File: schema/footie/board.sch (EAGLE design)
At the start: 35 parts, among them T1 2N3565, U1 ATMEGA328P-MU, U2 USD-SOCKETNEW, U3 HC_05, U4 MCP73831, U5 3.3 regulator, Y1 8MHZ

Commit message: complete the first pcb version
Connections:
- net GND renamed N$22
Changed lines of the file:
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@@
 </busses>
 <nets>
-<net name="GND" class="0">
+<net name="N$22" class="0">
 <segment>
 <pinref part="U$1" gate="G$1" pin="24_GND"/>

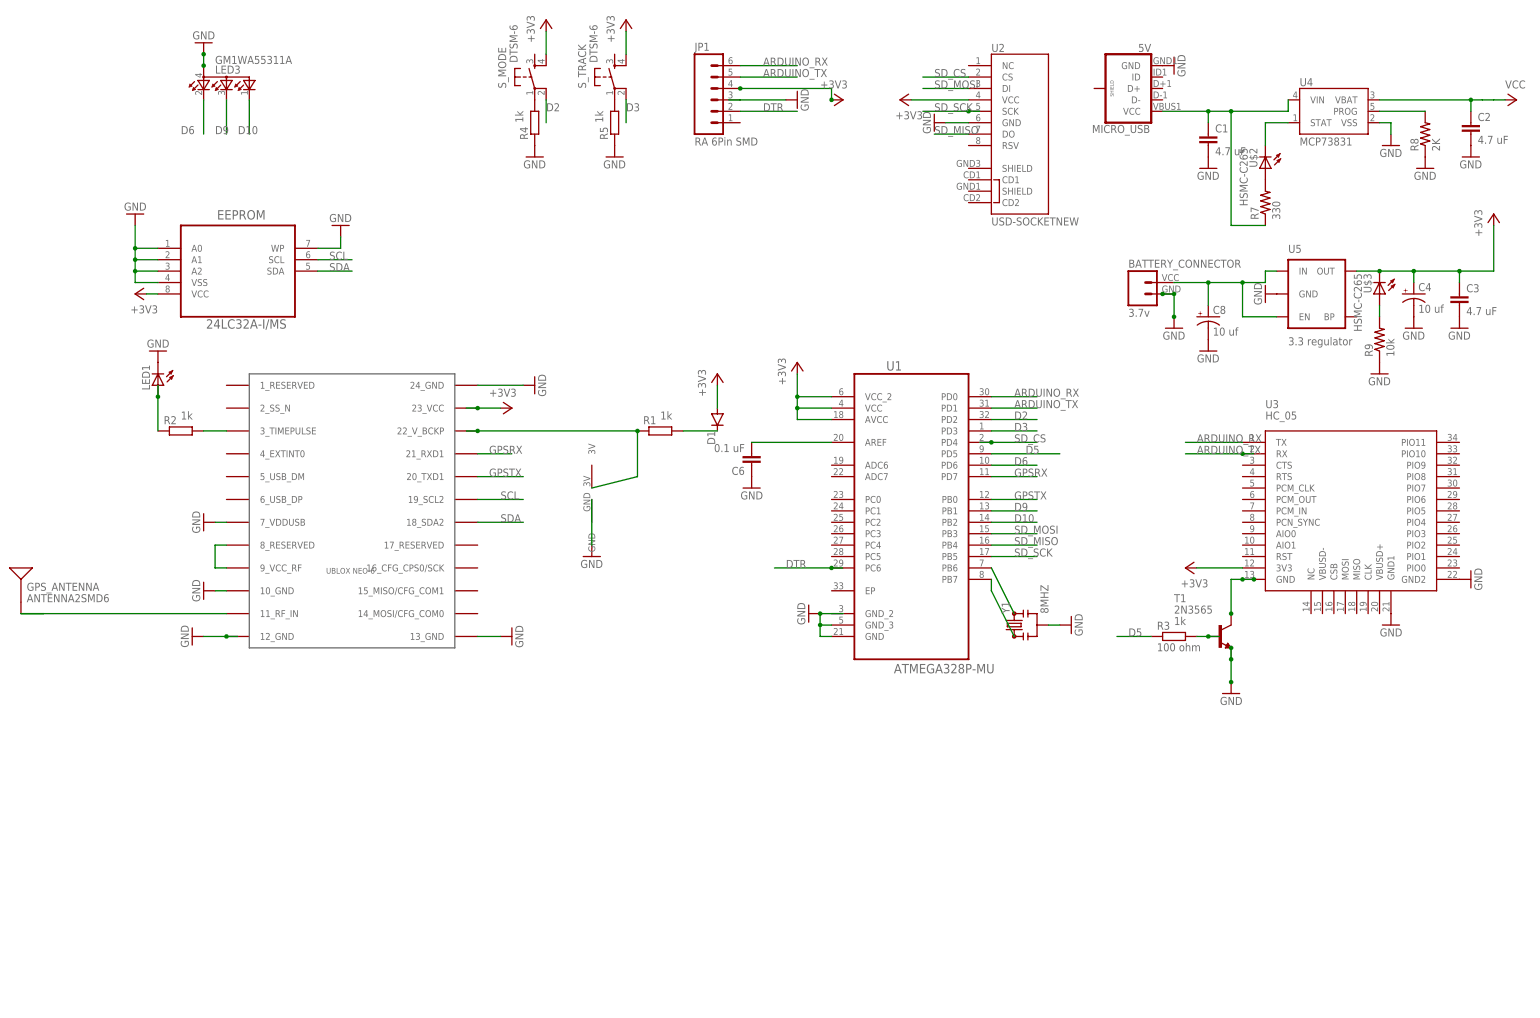
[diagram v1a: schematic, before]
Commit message: update items to 1206 package update cpu update library
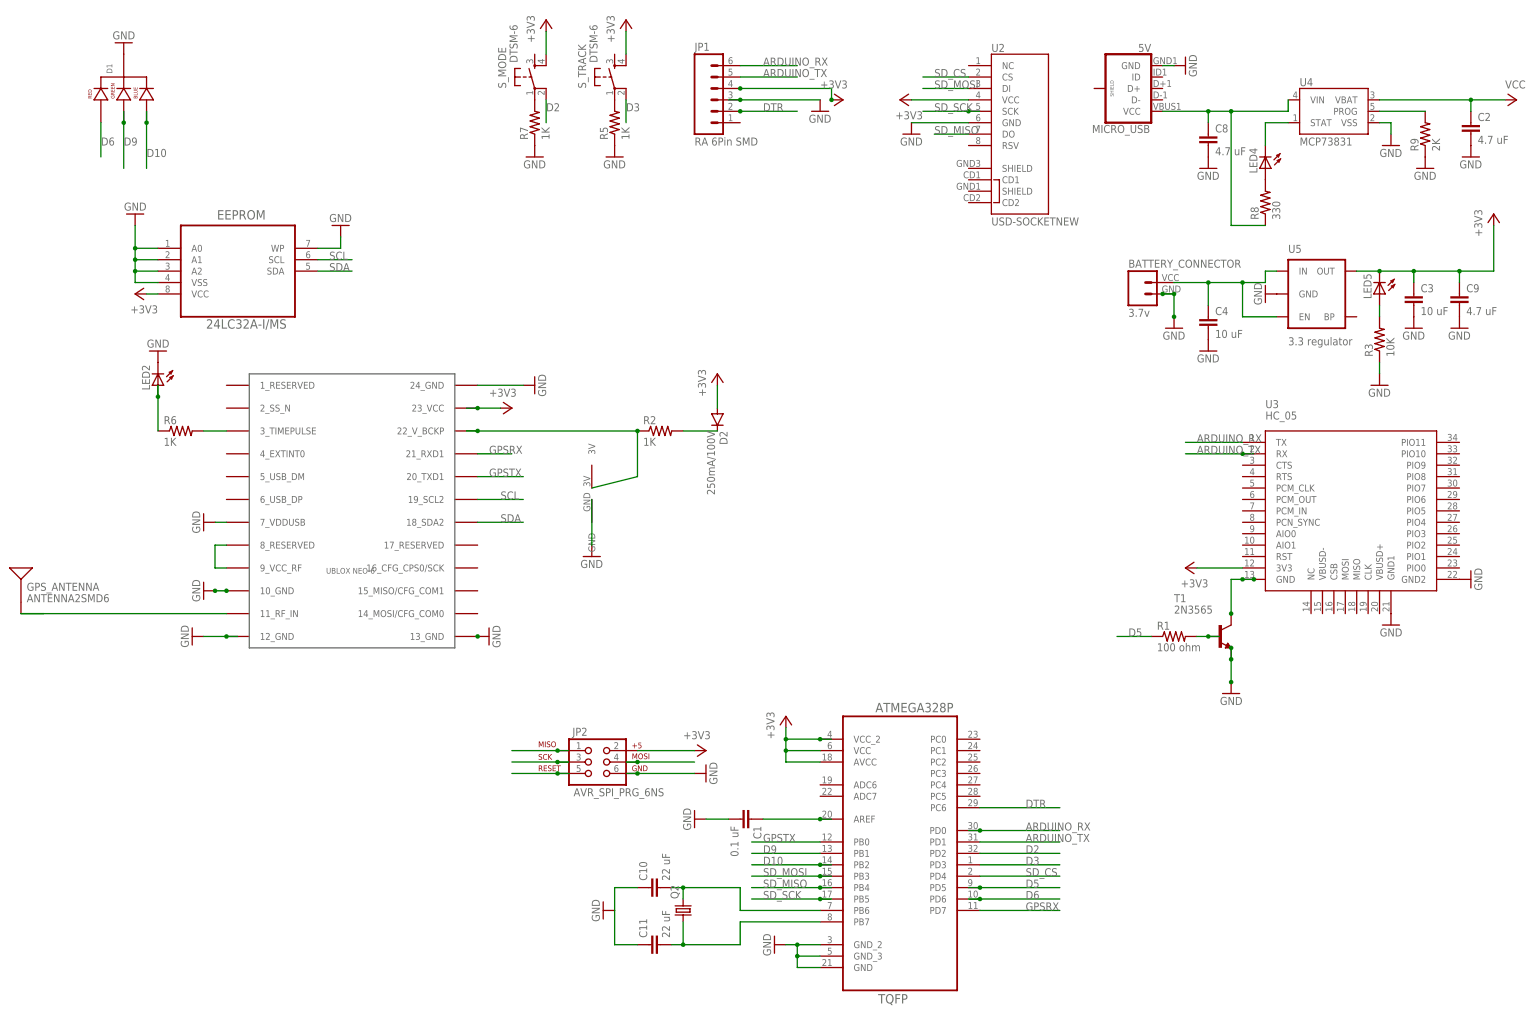
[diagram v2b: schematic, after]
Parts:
- removed C6: 0.1 uF, resistor:C-EUC0402K
- removed LED1: (no value), led:LEDCHIP-LED0805
- removed LED3: GM1WA55311A, led:GM1WA55311A
- removed R4: (no value), resistor:R-EU_M1406
- removed U$2, U$3: HSMC-C265, SparkFun-Retired:HSMC-C265
- removed U1: ATMEGA328P-MU, Atmel_By_element14_Batch_1-00:ATMEGA328P-MU
- removed Y1: 8MHZ, SparkFun-FreqCtrl:RESONATOR16MHZ
- added C10, C11: 22 uF, SparkFun-Capacitors:CAP1206
- added C9: 4.7 uF, SparkFun-Capacitors:CAP1206
- added D2: 250mA/100V, SparkFun-DiscreteSemi:DIODEBAS16
- added JP2: AVR_SPI_PRG_6NS, SparkFun-Connectors:AVR_SPI_PRG_6NS
- added LED2, LED4, LED5: (no value), eagle-ltspice:LED_E
- added Q2: (no value), crystal:CRYSTALCTS406
- added R6: 1K, SparkFun-Passives:RESISTOR1206
- added U6: ATMEGA328P-AU, Ava:ATMEGA328P-AU
- C1: value 4.7 uF -> 0.1 uF; device resistor:C-EUC0402K -> SparkFun-Capacitors:CAP1206
- C2: device resistor:C-EUC0402K -> SparkFun-Capacitors:CAP1206
- C3: value 4.7 uF -> 10 uF; device resistor:C-EUC0402K -> SparkFun-Capacitors:CAP1206
- C4: value 10 uf -> 10 uF; device resistor:CPOL-USA -> SparkFun-Capacitors:CAP1206
- C8: value 10 uf -> 4.7 uF; device resistor:CPOL-USA -> SparkFun-Capacitors:CAP1206
- D1: value (none) -> LED-RGB-CC-THRUCLEAR; device SparkFun-DiscreteSemi:DIODESMA -> SparkFun-LED:LED-RGB-CC-THRUCLEAR
- R1: value (none) -> 100 ohm; device resistor:R-EU_M1406 -> SparkFun-Passives:RESISTOR1206; OHM 1k -> (none)
- R2, R5: value (none) -> 1K; device resistor:R-EU_M1406 -> SparkFun-Passives:RESISTOR1206; OHM 1k -> (none)
- R3: value 100 ohm -> 10K; device resistor:R-EU_M1406 -> SparkFun-Passives:RESISTOR1206; OHM 1k -> (none)
- R7: value 330 -> 1K; device SparkFun-Passives:RESISTOR0402-RES -> SparkFun-Passives:RESISTOR1206
- R8: value 2K -> 330; device SparkFun-Passives:RESISTOR0402-RES -> SparkFun-Passives:RESISTOR1206
- R9: value 10k -> 2K; device SparkFun-Passives:RESISTOR0402-RES -> SparkFun-Passives:RESISTOR1206
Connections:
- removed net N$13: U1.PB7, Y1.1
- removed net N$14: U1.PB6, Y1.3
- removed net N$17: C6.2, U1.AREF
- new net GND: BATTERY_CONNECTOR.1, C1.2, C10.1, C11.1, C2.2, C3.2, C4.2, C8.2, C9.2, D1.CATHODE, EEPROM.A0, EEPROM.A1, EEPROM.A2, EEPROM.VSS, EEPROM.WP, JP1.3, JP2.6, LED2.C, MICRO_USB.GND, R3.1, R5.1, R7.1, R9.1, T1.E, U$1.10_GND, U$1.12_GND, U$1.13_GND, U$1.24_GND, U$1.7_VDDUSB, U$4.GND, U2.GND, U3.GND1, U3.GND2, U4.VSS, U5.GND, U6.GND, U6.GND_2, U6.GND_3
- new net N$27: C11.2, Q2.1, U6.PB7
- new net N$29: C10.2, Q2.2, U6.PB6
- net +3V3: now also C9.1, D2.A, JP2.2, LED5.C, U6.AVCC, U6.VCC, U6.VCC_2; no longer C4.+, D1.A, U$3.C, U1.AVCC, U1.VCC, U1.VCC_2
- net ARDUINO_RX: now also U6.PD0; no longer U1.PD0
- net ARDUINO_TX: now also U6.PD1; no longer U1.PD1
- net D10: now also D1.BLUE_CATHODE, U6.PB2; no longer LED3.CGREEN, U1.PB2
- net D2: now also U6.PD2; no longer U1.PD2
- net D3: now also U6.PD3; no longer U1.PD3
- net D5: now also R1.1, U6.PD5; no longer R3.1, U1.PD5
- net D6: now also D1.RED_CATHODE, U6.PD6; no longer LED3.CRED, U1.PD6
- net D9: now also D1.GREEN_CATHODE, U6.PB1; no longer LED3.CBLUE, U1.PB1
- net DTR: now also JP2.5, U6.PC6; no longer U1.PC6
- net GPSRX: now also U6.PD7; no longer U1.PD7
- net GPSTX: now also U6.PB0; no longer U1.PB0
- net N$1: now also D2.C, R2.2; no longer D1.C, R1.2
- net N$11: now also LED4.C; no longer U$2.C
- net N$12: now also C4.1; no longer C8.+
- net N$15: now also R9.2; no longer R8.2
- net N$16: now also LED5.A, R3.2; no longer R9.2, U$3.A
- net N$19: now also R1.2; no longer R3.2
- net N$2: now also C8.1, R8.1; no longer C1.1, R7.1
- net N$22: now also C1.1, U6.AREF; no longer BATTERY_CONNECTOR.1, C1.2, C2.2, C3.2, C4.-, C6.1, C8.-, EEPROM.A0, EEPROM.A1, EEPROM.A2, EEPROM.VSS, EEPROM.WP, JP1.3, LED1.C, LED3.A, MICRO_USB.GND, R4.1, R5.1, R8.1, R9.1, T1.E, U$1.10_GND, U$1.12_GND, U$1.13_GND, U$1.24_GND, U$1.7_VDDUSB, U$4.GND, U1.GND, U1.GND_2, U1.GND_3, U2.GND, U3.GND1, U3.GND2, U4.VSS, U5.GND, Y1.2
- net N$3: now also R6.2; no longer R2.2
- net N$4: now also LED2.A, R6.1; no longer LED1.A, R2.1
- net N$6: now also R2.1; no longer R1.1
- net N$8: now also LED4.A, R8.2; no longer R7.2, U$2.A
- net N$9: now also R7.2; no longer R4.2
- net SD_CS: now also U6.PD4; no longer U1.PD4
- net SD_MISO: now also JP2.1, U6.PB4; no longer U1.PB4
- net SD_MOSI: now also JP2.4, U6.PB3; no longer U1.PB3
- net SD_SCK: now also JP2.3, U6.PB5; no longer U1.PB5
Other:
- moved on the sheet: C1, C3, R7, R8, R9
